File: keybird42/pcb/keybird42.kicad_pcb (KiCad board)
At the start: 2 copper layers, 173 parts, among them SW111 SW_MX, SW112 SW_MX, SW113 SW_MX, SW114 SW_MX, SW115 SW_MX, SW116 SW_MX, SW117 SW_MX, SW121 SW_MX, SW122 SW_MX, SW123 SW_MX, SW124 SW_MX, SW125 SW_MX, SW126 SW_MX, SW127 SW_MX, SW131 SW_MX, SW132 SW_MX, SW133 SW_MX, SW134 SW_MX, SW135 SW_MX, SW136 SW_MX, SW137 SW_MX, SW211 SW_MX, SW212 SW_MX, SW213 SW_MX, SW214 SW_MX, SW215 SW_MX, SW216 SW_MX, SW217 SW_MX, SW221 SW_MX, SW222 SW_MX, SW223 SW_MX, SW225 SW_MX, SW226 SW_MX, SW227 SW_MX, SW231 SW_MX, SW232 SW_MX, SW233 SW_MX, SW234 SW_MX, SW235 SW_MX, SW236 SW_MX, SW237 SW_MX, SW311 SW_MX, SW312 SW_MX, SW314 SW_MX, SW315 SW_MX, SW316 SW_MX, SW317 SW_MX, SW321 SW_MX, SW322 SW_MX, SW323 SW_MX, SW324 SW_MX, SW325 SW_MX, SW327 SW_MX, SW331 SW_MX, SW332 SW_MX, SW333 SW_MX, SW334 SW_MX, SW335 SW_MX, SW336 SW_MX, SW337 SW_MX, SW411 SW_MX, SW412 SW_MX, SW413 SW_MX, SW414 SW_MX, SW415 SW_MX, SW416 SW_MX, SW417 SW_MX, SW421 SW_MX, SW423 SW_MX, SW424 SW_MX, SW425 SW_MX, SW426 SW_MX, SW427 SW_MX, SW431 SW_MX, SW432 SW_MX, SW433 SW_MX, SW434 SW_MX, SW436 SW_MX, SW437 SW_MX, SW501 SW_MX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

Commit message: diode reorg
swap pins of switches so diodes are wired to upper pads of sockets

change diodes to sod-123 because that's the commonly available kind

need to redo traces and vias
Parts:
- D111, D112, D113, D114, D115, D116, D117, D121, D122, D123, D124, D125, D126, D127, D131, D132, D133, D134, D135, D136, D137, D211, D212, D213, D214, D215, D216, D217, D221, D222, D223, D225, D226, D227, D231, D232, D233, D234, D235, D236, D237, D311, D312, D314, D315, D316, D317, D321, D322, D323, D324, D325, D327, D331, D332, D333, D334, D335, D336, D337, D411, D412, D413, D414, D415, D416, D417, D421, D423, D424, D425, D426, D427, D431, D432, D433, D434, D436, D437, D501, D502, D503, D504, D505, D506, D507: footprint keybird42:D_1206_HandSolder_Back -> keybird42:D_SOD-123_HandSolder_Back
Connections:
- SW111 pad 1: Net-(D111-A) -> /COL1
- SW111 pad 2: /COL1 -> Net-(D111-A)
- SW112 pad 1: Net-(D112-A) -> /COL2
- SW112 pad 2: /COL2 -> Net-(D112-A)
- SW113 pad 1: Net-(D113-A) -> /COL3
- SW113 pad 2: /COL3 -> Net-(D113-A)
- SW114 pad 1: Net-(D114-A) -> /COL4
- SW114 pad 2: /COL4 -> Net-(D114-A)
- SW115 pad 1: Net-(D115-A) -> /COL5
- SW115 pad 2: /COL5 -> Net-(D115-A)
- SW116 pad 1: Net-(D116-A) -> /COL6
- SW116 pad 2: /COL6 -> Net-(D116-A)
- SW117 pad 1: Net-(D117-A) -> /COL7
- SW117 pad 2: /COL7 -> Net-(D117-A)
- SW121 pad 1: Net-(D121-A) -> /COL1
- SW121 pad 2: /COL1 -> Net-(D121-A)
- SW122 pad 1: Net-(D122-A) -> /COL2
- SW122 pad 2: /COL2 -> Net-(D122-A)
- SW123 pad 1: Net-(D123-A) -> /COL3
- SW123 pad 2: /COL3 -> Net-(D123-A)
- SW124 pad 1: Net-(D124-A) -> /COL4
- SW124 pad 2: /COL4 -> Net-(D124-A)
- SW125 pad 1: Net-(D125-A) -> /COL5
- SW125 pad 2: /COL5 -> Net-(D125-A)
- SW126 pad 1: Net-(D126-A) -> /COL6
- SW126 pad 2: /COL6 -> Net-(D126-A)
- SW127 pad 1: Net-(D127-A) -> /COL7
- SW127 pad 2: /COL7 -> Net-(D127-A)
- SW131 pad 1: Net-(D131-A) -> /COL1
- SW131 pad 2: /COL1 -> Net-(D131-A)
- SW132 pad 1: Net-(D132-A) -> /COL2
- SW132 pad 2: /COL2 -> Net-(D132-A)
- SW133 pad 1: Net-(D133-A) -> /COL3
- SW133 pad 2: /COL3 -> Net-(D133-A)
- SW134 pad 1: Net-(D134-A) -> /COL4
- SW134 pad 2: /COL4 -> Net-(D134-A)
- SW135 pad 1: Net-(D135-A) -> /COL5
- SW135 pad 2: /COL5 -> Net-(D135-A)
- SW136 pad 1: Net-(D136-A) -> /COL6
- SW136 pad 2: /COL6 -> Net-(D136-A)
- SW137 pad 1: Net-(D137-A) -> /COL7
- SW137 pad 2: /COL7 -> Net-(D137-A)
- SW211 pad 1: Net-(D211-A) -> /COL1
- SW211 pad 2: /COL1 -> Net-(D211-A)
- SW212 pad 1: Net-(D212-A) -> /COL2
- SW212 pad 2: /COL2 -> Net-(D212-A)
- SW213 pad 1: Net-(D213-A) -> /COL3
- SW213 pad 2: /COL3 -> Net-(D213-A)
- SW214 pad 1: Net-(D214-A) -> /COL4
- SW214 pad 2: /COL4 -> Net-(D214-A)
- SW215 pad 1: Net-(D215-A) -> /COL5
- SW215 pad 2: /COL5 -> Net-(D215-A)
- SW216 pad 1: Net-(D216-A) -> /COL6
- SW216 pad 2: /COL6 -> Net-(D216-A)
- SW217 pad 1: Net-(D217-A) -> /COL7
- SW217 pad 2: /COL7 -> Net-(D217-A)
- SW221 pad 1: Net-(D221-A) -> /COL1
- SW221 pad 2: /COL1 -> Net-(D221-A)
- SW222 pad 1: Net-(D222-A) -> /COL2
- SW222 pad 2: /COL2 -> Net-(D222-A)
- SW223 pad 1: Net-(D223-A) -> /COL3
- SW223 pad 2: /COL3 -> Net-(D223-A)
- SW225 pad 1: Net-(D225-A) -> /COL5
- SW225 pad 2: /COL5 -> Net-(D225-A)
- SW226 pad 1: Net-(D226-A) -> /COL6
- SW226 pad 2: /COL6 -> Net-(D226-A)
- SW227 pad 1: Net-(D227-A) -> /COL7
- SW227 pad 2: /COL7 -> Net-(D227-A)
- SW231 pad 1: Net-(D231-A) -> /COL1
- SW231 pad 2: /COL1 -> Net-(D231-A)
- SW232 pad 1: Net-(D232-A) -> /COL2
- SW232 pad 2: /COL2 -> Net-(D232-A)
- SW233 pad 1: Net-(D233-A) -> /COL3
- SW233 pad 2: /COL3 -> Net-(D233-A)
- SW234 pad 1: Net-(D234-A) -> /COL4
- SW234 pad 2: /COL4 -> Net-(D234-A)
- SW235 pad 1: Net-(D235-A) -> /COL5
- SW235 pad 2: /COL5 -> Net-(D235-A)
- SW236 pad 1: Net-(D236-A) -> /COL6
- SW236 pad 2: /COL6 -> Net-(D236-A)
- SW237 pad 1: Net-(D237-A) -> /COL7
- SW237 pad 2: /COL7 -> Net-(D237-A)
- SW311 pad 1: Net-(D311-A) -> /COL1
- SW311 pad 2: /COL1 -> Net-(D311-A)
- SW312 pad 1: Net-(D312-A) -> /COL2
- SW312 pad 2: /COL2 -> Net-(D312-A)
- SW314 pad 1: Net-(D314-A) -> /COL4
- SW314 pad 2: /COL4 -> Net-(D314-A)
- SW315 pad 1: Net-(D315-A) -> /COL5
- SW315 pad 2: /COL5 -> Net-(D315-A)
- SW316 pad 1: Net-(D316-A) -> /COL6
- SW316 pad 2: /COL6 -> Net-(D316-A)
- SW317 pad 1: Net-(D317-A) -> /COL7
- SW317 pad 2: /COL7 -> Net-(D317-A)
- SW321 pad 1: Net-(D321-A) -> /COL1
- SW321 pad 2: /COL1 -> Net-(D321-A)
- SW322 pad 1: Net-(D322-A) -> /COL2
- SW322 pad 2: /COL2 -> Net-(D322-A)
- SW323 pad 1: Net-(D323-A) -> /COL3
- SW323 pad 2: /COL3 -> Net-(D323-A)
- SW324 pad 1: Net-(D324-A) -> /COL4
- SW324 pad 2: /COL4 -> Net-(D324-A)
- SW325 pad 1: Net-(D325-A) -> /COL5
- SW325 pad 2: /COL5 -> Net-(D325-A)
- SW327 pad 1: Net-(D327-A) -> /COL7
- SW327 pad 2: /COL7 -> Net-(D327-A)
- SW331 pad 1: Net-(D331-A) -> /COL1
- SW331 pad 2: /COL1 -> Net-(D331-A)
- SW332 pad 1: Net-(D332-A) -> /COL2
- SW332 pad 2: /COL2 -> Net-(D332-A)
- SW333 pad 1: Net-(D333-A) -> /COL3
- SW333 pad 2: /COL3 -> Net-(D333-A)
- SW334 pad 1: Net-(D334-A) -> /COL4
- SW334 pad 2: /COL4 -> Net-(D334-A)
- SW335 pad 1: Net-(D335-A) -> /COL5
- SW335 pad 2: /COL5 -> Net-(D335-A)
- SW336 pad 1: Net-(D336-A) -> /COL6
- SW336 pad 2: /COL6 -> Net-(D336-A)
- SW337 pad 1: Net-(D337-A) -> /COL7
- SW337 pad 2: /COL7 -> Net-(D337-A)
- SW411 pad 1: Net-(D411-A) -> /COL1
- SW411 pad 2: /COL1 -> Net-(D411-A)
- SW412 pad 1: Net-(D412-A) -> /COL2
- SW412 pad 2: /COL2 -> Net-(D412-A)
- SW413 pad 1: Net-(D413-A) -> /COL3
- SW413 pad 2: /COL3 -> Net-(D413-A)
- SW414 pad 1: Net-(D414-A) -> /COL4
- SW414 pad 2: /COL4 -> Net-(D414-A)
- SW415 pad 1: Net-(D415-A) -> /COL5
- SW415 pad 2: /COL5 -> Net-(D415-A)
- SW416 pad 1: Net-(D416-A) -> /COL6
- SW416 pad 2: /COL6 -> Net-(D416-A)
- SW417 pad 1: Net-(D417-A) -> /COL7
- SW417 pad 2: /COL7 -> Net-(D417-A)
- SW421 pad 1: Net-(D421-A) -> /COL1
- SW421 pad 2: /COL1 -> Net-(D421-A)
- SW423 pad 1: Net-(D423-A) -> /COL3
- SW423 pad 2: /COL3 -> Net-(D423-A)
- SW424 pad 1: Net-(D424-A) -> /COL4
- SW424 pad 2: /COL4 -> Net-(D424-A)
- SW425 pad 1: Net-(D425-A) -> /COL5
- SW425 pad 2: /COL5 -> Net-(D425-A)
- SW426 pad 1: Net-(D426-A) -> /COL6
- SW426 pad 2: /COL6 -> Net-(D426-A)
- SW427 pad 1: Net-(D427-A) -> /COL7
- SW427 pad 2: /COL7 -> Net-(D427-A)
- SW431 pad 1: Net-(D431-A) -> /COL1
- SW431 pad 2: /COL1 -> Net-(D431-A)
- SW432 pad 1: Net-(D432-A) -> /COL2
- SW432 pad 2: /COL2 -> Net-(D432-A)
- SW433 pad 1: Net-(D433-A) -> /COL3
- SW433 pad 2: /COL3 -> Net-(D433-A)
- SW434 pad 1: Net-(D434-A) -> /COL4
- SW434 pad 2: /COL4 -> Net-(D434-A)
- SW436 pad 1: Net-(D436-A) -> /COL6
- SW436 pad 2: /COL6 -> Net-(D436-A)
- SW437 pad 1: Net-(D437-A) -> /COL7
- SW437 pad 2: /COL7 -> Net-(D437-A)
- SW501 pad 1: Net-(D501-A) -> /COL1
- SW501 pad 2: /COL1 -> Net-(D501-A)
- SW502 pad 1: Net-(D502-A) -> /COL2
- SW502 pad 2: /COL2 -> Net-(D502-A)
- SW503 pad 1: Net-(D503-A) -> /COL3
- SW503 pad 2: /COL3 -> Net-(D503-A)
- SW504 pad 1: Net-(D504-A) -> /COL4
- SW504 pad 2: /COL4 -> Net-(D504-A)
- SW505 pad 1: Net-(D505-A) -> /COL5
- SW505 pad 2: /COL5 -> Net-(D505-A)
- SW506 pad 1: Net-(D506-A) -> /COL6
- SW506 pad 2: /COL6 -> Net-(D506-A)
- SW507 pad 1: Net-(D507-A) -> /COL7
- SW507 pad 2: /COL7 -> Net-(D507-A)
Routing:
- net /COL1: track 31.4 -> 0.00 mm, vias 13 -> 0
- net /COL7: track 31.4 -> 0.00 mm, vias 13 -> 0
- net /COL5: track 29.0 -> 0.00 mm, vias 12 -> 0
- net /COL3: track 29.0 -> 0.00 mm, vias 12 -> 0
- net /COL6: track 29.0 -> 0.00 mm, vias 12 -> 0
- net /COL2: track 29.0 -> 0.00 mm, vias 12 -> 0
- net /COL4: track 29.0 -> 0.00 mm, vias 12 -> 0
- net /ROW50: track 11.8 -> 0.00 mm, vias 7 -> 0
- net /ROW41: track 11.8 -> 0.00 mm, vias 7 -> 0
- net /ROW33: track 11.8 -> 0.00 mm, vias 7 -> 0
- net /ROW23: track 11.8 -> 0.00 mm, vias 7 -> 0
- net /ROW21: track 11.8 -> 0.00 mm, vias 7 -> 0
- net /ROW13: track 11.8 -> 0.00 mm, vias 7 -> 0
- net /ROW12: track 11.8 -> 0.00 mm, vias 7 -> 0
- net /ROW11: track 11.8 -> 0.00 mm, vias 7 -> 0
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
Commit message: fix diode placement
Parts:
- moved D112 8.52 mm to (102.9, 25.4)
- moved D113 8.52 mm to (160.0, 25.4)
- moved D115 8.52 mm to (274.3, 25.4)
- moved D116 8.52 mm to (331.5, 25.4)
- moved D117 8.52 mm to (395.0, 31.8)
- moved D121 8.52 mm to (58.4, 31.8)
- moved D122 8.52 mm to (121.9, 25.4)
- moved D123 8.52 mm to (179.1, 25.4)
- moved D124 8.52 mm to (236.2, 25.4)
- moved D125 8.52 mm to (293.4, 25.4)
- moved D126 8.52 mm to (350.5, 25.4)
- moved D127 8.52 mm to (414.0, 31.8)
- moved D131 8.52 mm to (77.5, 31.8)
- moved D132 8.52 mm to (141.0, 25.4)
- moved D133 8.52 mm to (198.1, 25.4)
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
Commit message: switches in the right places now, i think
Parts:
- moved U1 62.6 mm to (261.9, 104.1)
- moved SW412 10.2 mm to (107.2, 85.7)
- moved D412 10.2 mm to (114.8, 85.7)
- moved D312 7.53 mm to (110.0, 66.7)
- moved SW312 7.53 mm to (102.4, 66.7)
- moved D506 6.40 mm to (343.4, 104.8)
- moved SW506 6.40 mm to (335.8, 104.8)
- moved D502 6.40 mm to (129.1, 104.8)
- moved SW502 6.40 mm to (121.4, 104.8)
- moved D503 5.72 mm to (155.3, 104.8)
- moved SW503 5.72 mm to (147.6, 104.8)
- moved D505 5.72 mm to (317.2, 104.8)
- moved SW505 5.72 mm to (309.6, 104.8)
- moved D501 5.08 mm to (105.3, 104.8)
- moved D507 5.08 mm to (367.2, 104.8)
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
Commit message: align diodes to 750/32 mil grid
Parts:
- moved D117 0.12 mm to (393.5, 33.3)
- moved D217 0.12 mm to (393.5, 52.4)
- moved D317 0.12 mm to (393.5, 76.2)
- moved D127 0.12 mm to (412.6, 33.3)
- moved D137 0.12 mm to (431.6, 33.3)
- moved D227 0.12 mm to (412.6, 52.4)
- moved D237 0.12 mm to (431.6, 52.4)
- moved D327 0.12 mm to (412.6, 76.2)
- moved D337 0.12 mm to (431.6, 76.2)
- moved D112 0.12 mm to (103.0, 28.6)
- moved D113 0.12 mm to (160.1, 28.6)
- moved D114 0.12 mm to (217.3, 28.6)
- moved D115 0.12 mm to (274.4, 28.6)
- moved D116 0.12 mm to (331.6, 28.6)
- moved D122 0.12 mm to (122.0, 28.6)
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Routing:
- net Net-(D111-A): track 0.00 -> 3.79 mm
- net /COL1: track 0.00 -> 2.56 mm, vias 0 -> 1
- net /ROW11: track 0.00 -> 1.80 mm, vias 0 -> 1

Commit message: fix silkscreen text on back
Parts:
- moved U1 0.56 mm to (261.9, 103.6)
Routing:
- net /COL7: track 0.00 -> 33.3 mm, vias 0 -> 13
- net /COL1: track 2.56 -> 33.3 mm, vias 1 -> 13
- net /COL6: track 0.00 -> 30.8 mm, vias 0 -> 12
- net /COL2: track 0.00 -> 30.8 mm, vias 0 -> 12
- net /COL5: track 0.00 -> 30.8 mm, vias 0 -> 12
- net /COL3: track 0.00 -> 30.8 mm, vias 0 -> 12
- net /COL4: track 0.00 -> 30.8 mm, vias 0 -> 12
- net /ROW50: track 0.00 -> 12.6 mm, vias 0 -> 7
- net /ROW13: track 0.00 -> 12.6 mm, vias 0 -> 7
- net /ROW12: track 0.00 -> 12.6 mm, vias 0 -> 7
- net /ROW23: track 0.00 -> 12.6 mm, vias 0 -> 7
- net /ROW21: track 0.00 -> 12.6 mm, vias 0 -> 7
- net /ROW41: track 0.00 -> 12.6 mm, vias 0 -> 7
- net /ROW33: track 0.00 -> 12.6 mm, vias 0 -> 7
- net /ROW11: track 1.80 -> 12.6 mm, vias 1 -> 7
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
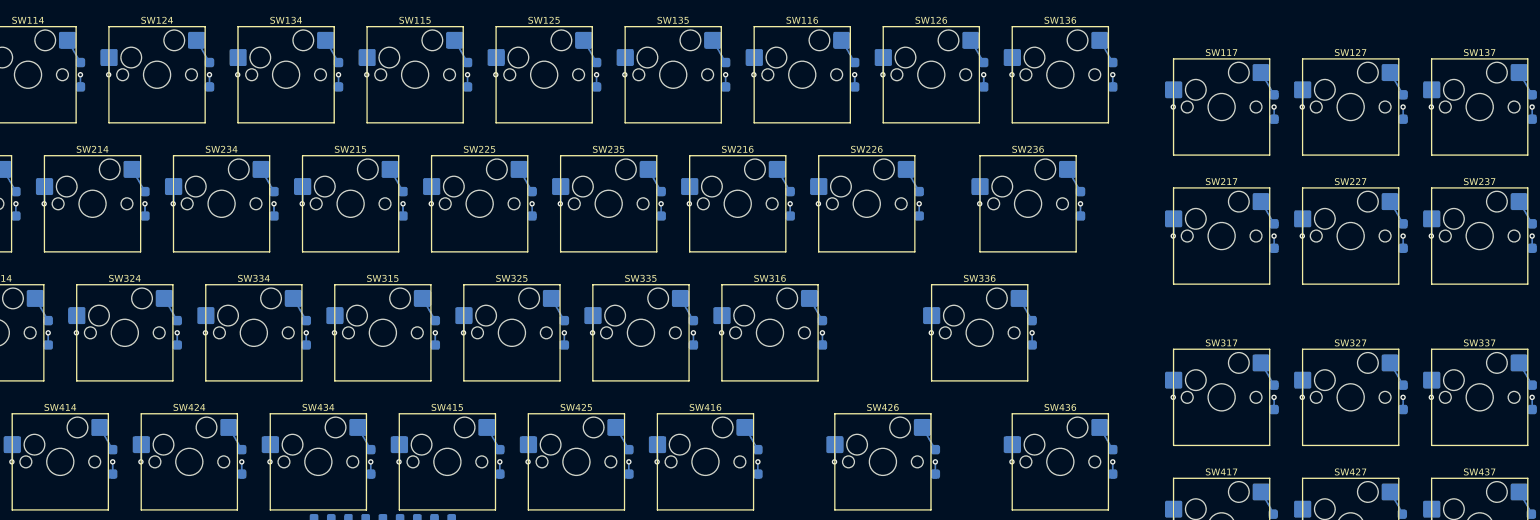
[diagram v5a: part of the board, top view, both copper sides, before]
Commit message: mirror switch row numbers
should make a nicer pattern of vias
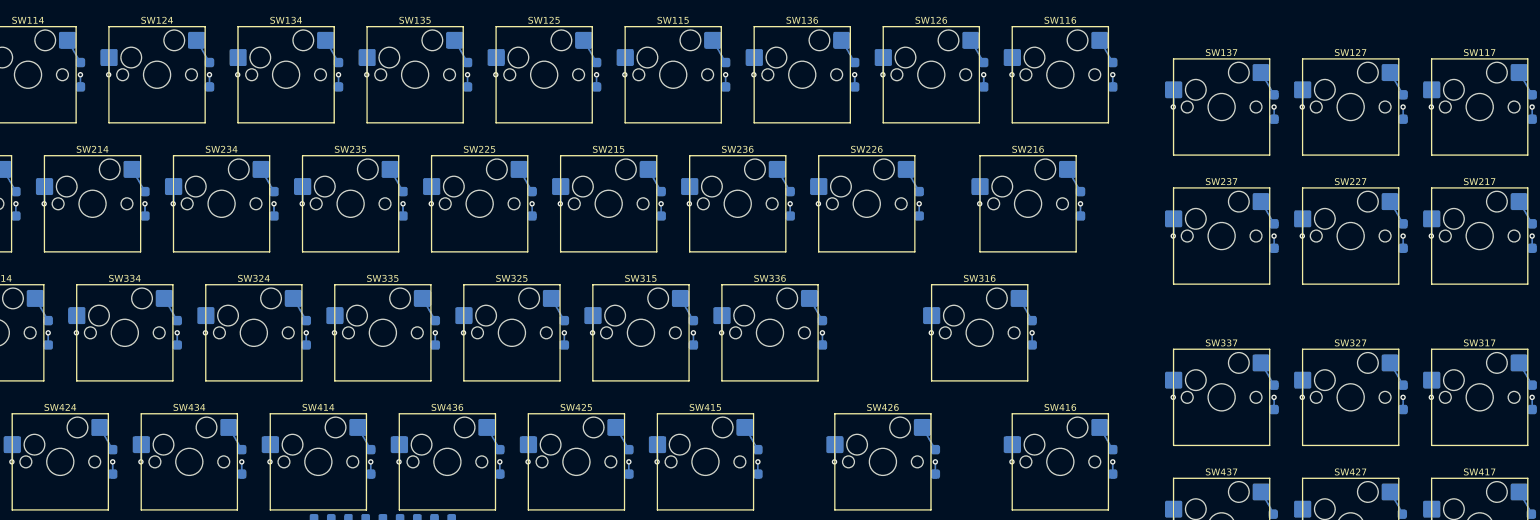
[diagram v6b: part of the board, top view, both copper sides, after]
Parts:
- moved D436 90.5 mm to (279.2, 85.7)
- moved SW436 90.5 mm to (271.5, 85.7)
- moved D416 52.4 mm to (369.7, 85.7)
- moved SW416 52.4 mm to (361.9, 85.7)
- moved D216 42.9 mm to (364.9, 47.6)
- moved D236 42.9 mm to (322.1, 47.6)
- moved SW216 42.9 mm to (357.2, 47.6)
- moved SW236 42.9 mm to (314.3, 47.6)
- moved D115 38.1 mm to (312.5, 28.6)
- moved D135 38.1 mm to (274.4, 28.6)
- moved D315 38.1 mm to (307.8, 66.7)
- moved D335 38.1 mm to (269.7, 66.7)
- moved D414 38.1 mm to (260.2, 85.7)
- moved D415 38.1 mm to (317.3, 85.7)
- moved D417 38.1 mm to (431.5, 95.2)
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
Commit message: add stabilizer mounting holes
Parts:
- added REF**: Stabilizer_Cherry_MX_2.00u, PCM_Mounting_Keyboard_Stabilizer:Stabilizer_Cherry_MX_2.00u, F.Cu at (350.0, 66.7)
- added REF**: Stabilizer_Cherry_MX_7.00u, PCM_Mounting_Keyboard_Stabilizer:Stabilizer_Cherry_MX_7.00u, F.Cu at (228.6, 104.8)
- added REF**: Stabilizer_Cherry_MX_2.00u, PCM_Mounting_Keyboard_Stabilizer:Stabilizer_Cherry_MX_2.00u, F.Cu at (107.2, 85.7)
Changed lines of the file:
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@@
     )
   )
+  (footprint "PCM_Mounting_Keyboard_Stabilizer:Stabilizer_Cherry_MX_2.00u" (layer "F.Cu")
+    (at 350.04375 66.675 180)
+    (descr "Cherry MX PCB Stabilizer 2.00u 2.25u 2.50u 2.75u")
+    (tags "Cherry MX Keyboard Stabilizer 2.00u 2.25u 2.50u 2.75u Cutout")
+    (attr exclude_from_pos_files exclude_from_bom)
+    (fp_text reference "REF**" (at 0 -2) (layer "F.SilkS") hide
+        (effects (font (size 1 1) (thickness 0.15)))
+    )
+    (fp_text value "Stabilizer_Cherry_MX_2.00u" (at 0 2) (layer "F.Fab") hide
+        (effects (font (size 1 1) (thickness 0.15)))
+    )
+    (fp_text user "${REFERENCE}" (at 0 0) (layer "F.Fab") hide
+        (effects (font (size 1 1) (thickness 0.15)))
+    )
+    (fp_line (start -15.313 -5.53) (end -15.313 6.77)
+      (stroke (width 0.1) (type solid)) (layer "Eco1.User"))
+    (fp_line (start -15.313 6.77) (end -8.563 6.77)
+      (stroke (width 0.1) (type solid)) (layer "Eco1.User"))
+    (fp_line (start -8.563 -5.53) (end -15.313 -5.53)
+      (stroke (width 0.1) (type solid)) (layer "Eco1.User"))
+    (fp_line (start -8.563 6.77) (end -8.563 -5.53)
+      (stroke (width 0.1) (type solid)) (layer "Eco1.User"))
+    (fp_line (start 8.563 -5.53) (end 8.563 6.77)
+      (stroke (width 0.1) (type solid)) (layer "Eco1.User"))
+    (fp_line (start 8.563 6.77) (end 15.313 6.77)
+      (stroke (width 0.1) (type solid)) (layer "Eco1.User"))
+    (fp_line (start 15.313 -5.53) (end 8.563 -5.53)
+      (stroke (width 0.1) (type solid)) (layer "Eco1.User"))
+    (fp_line (start 15.313 6.77) (end 15.313 -5.53)
+      (stroke (width 0.1) (type solid)) (layer "Eco1.User"))
+    (pad "" np_thru_hole circle (at -11.938 -6.985 180) (size 3.048 3.048) (drill 3.048) (layers "*.Cu" "*.Mask"))
+    (pad "" np_thru_hole circle (at -11.938 8.225 180) (size 3.9878 3.9878) (drill 3.9878) (layers "*.Cu" "*.Mask"))
+    (pad "" np_thru_hole circle (at 11.938 -6.985 180) (size 3.048 3.048) (drill 3.048) (layers "*.Cu" "*.Mask"))
+    (pad "" np_thru_hole circle (at 11.938 8.225 180) (size 3.9878 3.9878) (drill 3.9878) (layers "*.Cu" "*.Mask"))
+    (model "${KICAD6_3RD_PARTY}/3dmodels/com_github_perigoso_keyswitch-kicad-library/3d-library.3dshapes/Stabilizer_Cherry_MX_2.00u.wrl"
+      (offset (xyz 0 0 0))
+      (scale (xyz 1 1 1))
+      (rotate (xyz 0 0 0))
+    )
+  )
+  (footprint "PCM_Mounting_Keyboard_Stabilizer:Stabilizer_Cherry_MX_7.00u" (layer "F.Cu")
+    (at 228.6 104.775 180)
+    (descr "Cherry MX PCB Stabilizer 7.00u")
+    (tags "Cherry MX Keyboard Stabilizer 7.00u Cutout")
+    (attr exclude_from_pos_files exclude_from_bom)
+    (fp_text reference "REF**" (at 0 -2) (layer "F.SilkS") hide
+        (effects (font (size 1 1) (thickness 0.15)))
+    )
+    (fp_text value "Stabilizer_Cherry_MX_7.00u" (at 0 2) (layer "F.Fab") hide
+        (effects (font (size 1 1) (thickness 0.15)))
+    )
+    (fp_text user "${REFERENCE}" (at 0 0) (layer "F.Fab") hide
+        (effects (font (size 1 1) (thickness 0.15)))
+    )
+    (fp_line (start -60.525 -5.53) (end -60.525 6.77)
+      (stroke (width 0.1) (type solid)) (layer "Eco1.User"))
+    (fp_line (start -60.525 6.77) (end -53.775 6.77)
+      (stroke (width 0.1) (type solid)) (layer "Eco1.User"))
+    (fp_line (start -53.775 -5.53) (end -60.525 -5.53)
+      (stroke (width 0.1) (type solid)) (layer "Eco1.User"))
+    (fp_line (start -53.775 6.77) (end -53.775 -5.53)
+      (stroke (width 0.1) (type solid)) (layer "Eco1.User"))
+    (fp_line (start 53.775 -5.53) (end 53.775 6.77)
+      (stroke (width 0.1) (type solid)) (layer "Eco1.User"))
+    (fp_line (start 53.775 6.77) (end 60.525 6.77)
+      (stroke (width 0.1) (type solid)) (layer "Eco1.User"))
+    (fp_line (start 60.525 -5.53) (end 53.775 -5.53)
+      (stroke (width 0.1) (type solid)) (layer "Eco1.User"))
+    (fp_line (start 60.525 6.77) (end 60.525 -5.53)
+      (stroke (width 0.1) (type solid)) (layer "Eco1.User"))
+    (pad "" np_thru_hole circle (at -57.15 -6.985 180) (size 3.048 3.048) (drill 3.048) (layers "*.Cu" "*.Mask"))
+    (pad "" np_thru_hole circle (at -57.15 8.225 180) (size 3.9878 3.9878) (drill 3.9878) (layers "*.Cu" "*.Mask"))
+    (pad "" np_thru_hole circle (at 57.15 -6.985 180) (size 3.048 3.048) (drill 3.048) (layers "*.Cu" "*.Mask"))
+    (pad "" np_thru_hole circle (at 57.15 8.225 180) (size 3.9878 3.9878) (drill 3.9878) (layers "*.Cu" "*.Mask"))
+    (model "${KICAD6_3RD_PARTY}/3dmodels/com_github_perigoso_keyswitch-kicad-library/3d-library.3dshapes/Stabilizer_Cherry_MX_7.00u.wrl"
+      (offset (xyz 0 0 0))
+      (scale (xyz 1 1 1))
+      (rotate (xyz 0 0 0))
+    )
+  )
   (footprint "PCM_Switch_Keyboard_Hotswap_Kailh:SW_Hotswap_Kailh_MX" (layer "F.Cu")
     (at 357.1875 47.625)
@@
       (offset (xyz 0 0 0))
       (scale (xyz 1 1 1))
+      (rotate (xyz 0 0 0))
+    )
+  )
+  (footprint "PCM_Mounting_Keyboard_Stabilizer:Stabilizer_Cherry_MX_2.00u" (layer "F.Cu")
+    (at 107.15625 85.725 180)
+    (descr "Cherry MX PCB Stabilizer 2.00u 2.25u 2.50u 2.75u")
+    (tags "Cherry MX Keyboard Stabilizer 2.00u 2.25u 2.50u 2.75u Cutout")
+    (attr exclude_from_pos_files exclude_from_bom)
+    (fp_text reference "REF**" (at 0 -2) (layer "F.SilkS") hide
+        (effects (font (size 1 1) (thickness 0.15)))
+    )
+    (fp_text value "Stabilizer_Cherry_MX_2.00u" (at 0 2) (layer "F.Fab") hide
+        (effects (font (size 1 1) (thickness 0.15)))
+    )
+    (fp_text user "${REFERENCE}" (at 0 0) (layer "F.Fab") hide
+        (effects (font (size 1 1) (thickness 0.15)))
+    )
+    (fp_line (start -15.313 -5.53) (end -15.313 6.77)
+      (stroke (width 0.1) (type solid)) (layer "Eco1.User"))
+    (fp_line (start -15.313 6.77) (end -8.563 6.77)
+      (stroke (width 0.1) (type solid)) (layer "Eco1.User"))
+    (fp_line (start -8.563 -5.53) (end -15.313 -5.53)
+      (stroke (width 0.1) (type solid)) (layer "Eco1.User"))
+    (fp_line (start -8.563 6.77) (end -8.563 -5.53)
+      (stroke (width 0.1) (type solid)) (layer "Eco1.User"))
+    (fp_line (start 8.563 -5.53) (end 8.563 6.77)
+      (stroke (width 0.1) (type solid)) (layer "Eco1.User"))
+    (fp_line (start 8.563 6.77) (end 15.313 6.77)
+      (stroke (width 0.1) (type solid)) (layer "Eco1.User"))
+    (fp_line (start 15.313 -5.53) (end 8.563 -5.53)
+      (stroke (width 0.1) (type solid)) (layer "Eco1.User"))
+    (fp_line (start 15.313 6.77) (end 15.313 -5.53)
+      (stroke (width 0.1) (type solid)) (layer "Eco1.User"))
+    (pad "" np_thru_hole circle (at -11.938 -6.985 180) (size 3.048 3.048) (drill 3.048) (layers "*.Cu" "*.Mask"))
+    (pad "" np_thru_hole circle (at -11.938 8.225 180) (size 3.9878 3.9878) (drill 3.9878) (layers "*.Cu" "*.Mask"))
+    (pad "" np_thru_hole circle (at 11.938 -6.985 180) (size 3.048 3.048) (drill 3.048) (layers "*.Cu" "*.Mask"))
+    (pad "" np_thru_hole circle (at 11.938 8.225 180) (size 3.9878 3.9878) (drill 3.9878) (layers "*.Cu" "*.Mask"))
+    (model "${KICAD6_3RD_PARTY}/3dmodels/com_github_perigoso_keyswitch-kicad-library/3d-library.3dshapes/Stabilizer_Cherry_MX_2.00u.wrl"
+      (offset (xyz 0 0 0))
+      (scale (xyz 1 1 1))

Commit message: horizontal busses in place
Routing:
- net (no net): track 0.00 -> 8321.0 mm
